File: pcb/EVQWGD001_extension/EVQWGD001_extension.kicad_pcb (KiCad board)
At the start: 2 copper layers, 16.8 x 19.3 mm, 6 parts, among them J1 Conn_01x01_MountingPin, J2 Conn_01x01_MountingPin, J3 Conn_01x01_MountingPin, J4 Conn_01x01_MountingPin, J5 Conn_01x01_MountingPin, SW1 RotaryEncoder_Switch

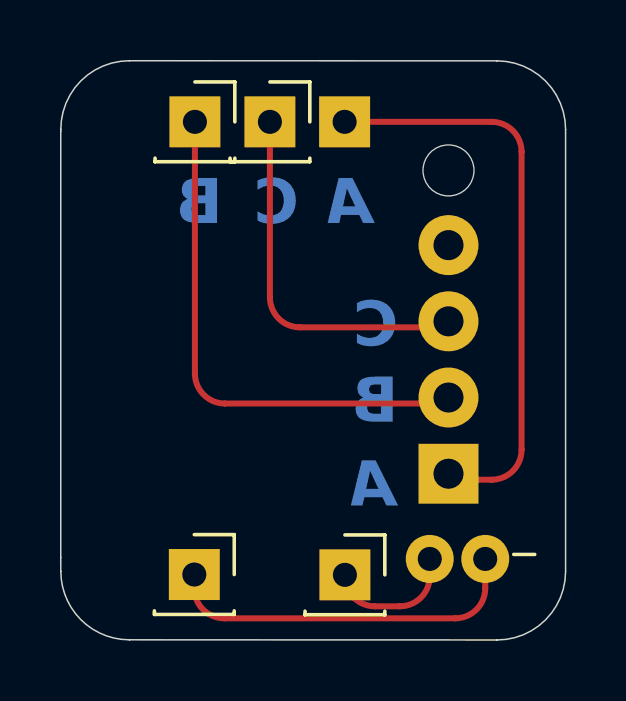
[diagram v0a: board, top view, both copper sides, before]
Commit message: add fp and symbol
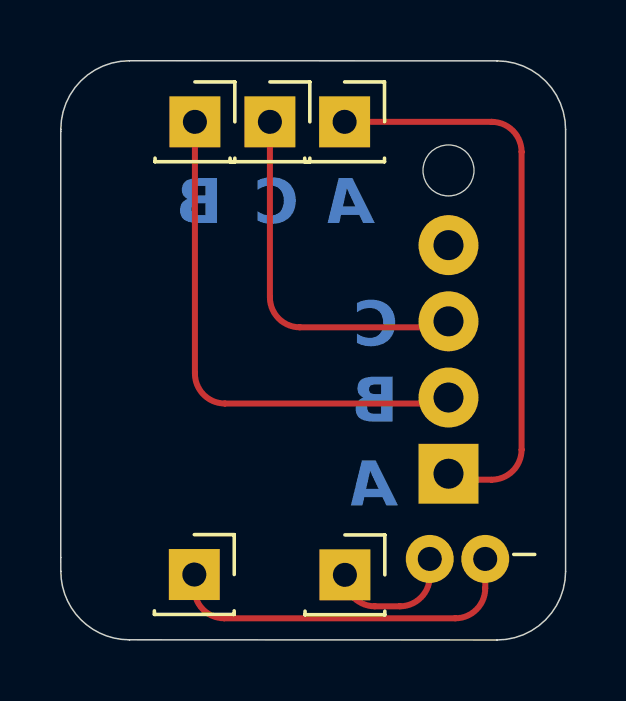
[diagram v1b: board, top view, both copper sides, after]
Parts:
- J1, J2, J3, J4, J5: footprint Connector_PinSocket_2.54mm:PinSocket_1x01_P2.54mm_Vertical -> roBa:PinSocket_1x01_P2.54mm_Vertical
- SW1: footprint EVQWGD001:EVQWGD001 -> roBa:EVQWGD001
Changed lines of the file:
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@@
 	(net 4 "Net-(J4-Pin_1)")
 	(net 5 "Net-(J5-Pin_1)")
-	(footprint "Connector_PinSocket_2.54mm:PinSocket_1x01_P2.54mm_Vertical"
+	(footprint "roBa:PinSocket_1x01_P2.54mm_Vertical"
 		(layer "F.Cu")
 		(at 149.95 93.98)
@@
 			)
 		)
-		(property "Footprint" "Connector_PinSocket_2.54mm:PinSocket_1x01_P2.54mm_Vertical"
+		(property "Footprint" "roBa:PinSocket_1x01_P2.54mm_Vertical"
 			(at 0 0 0)
 			(unlocked yes)
@@
 			)
 		)
+		(property ki_fp_filters "Connector*:*_1x??-1MP*")
+		(sheetname "ルート")
+		(sheetfile "EVQWGD001_extension.kicad_sch")
 		(attr through_hole)
 		(fp_line
@@
 		)
 	)
-	(footprint "Connector_PinSocket_2.54mm:PinSocket_1x01_P2.54mm_Vertical"
+	(footprint "roBa:PinSocket_1x01_P2.54mm_Vertical"
 		(layer "F.Cu")
 		(at 149.93 109.07)
@@
 			)
 		)
-		(property "Footprint" "Connector_PinSocket_2.54mm:PinSocket_1x01_P2.54mm_Vertical"
+		(property "Footprint" "roBa:PinSocket_1x01_P2.54mm_Vertical"
 			(at 0 0 0)
 			(unlocked yes)
@@
 			)
 		)
+		(property ki_fp_filters "Connector*:*_1x??-1MP*")
+		(sheetname "ルート")
+		(sheetfile "EVQWGD001_extension.kicad_sch")
 		(attr through_hole)
 		(fp_line
@@
 		)
 	)
-	(footprint "Connector_PinSocket_2.54mm:PinSocket_1x01_P2.54mm_Vertical"
+	(footprint "roBa:PinSocket_1x01_P2.54mm_Vertical"
 		(layer "F.Cu")
 		(at 152.45 93.98)
@@
 			)
 		)
-		(property "Footprint" "Connector_PinSocket_2.54mm:PinSocket_1x01_P2.54mm_Vertical"
+		(property "Footprint" "roBa:PinSocket_1x01_P2.54mm_Vertical"
 			(at 0 0 0)
 			(unlocked yes)
@@
 			)
 		)
+		(property ki_fp_filters "Connector*:*_1x??-1MP*")
+		(sheetname "ルート")
+		(sheetfile "EVQWGD001_extension.kicad_sch")
 		(attr through_hole)
 		(fp_line
@@
 		)
 	)
-	(footprint "EVQWGD001:EVQWGD001"
+	(footprint "roBa:EVQWGD001"
 		(layer "F.Cu")
 		(at 151.518 101.4 180)
@@
 			)
 		)
-		(property "Footprint" "EVQWGD001:EVQWGD001"
+		(property "Footprint" "roBa:EVQWGD001"
 			(at 1.64 -2.44 0)
 			(unlocked yes)
@@
 			)
 		)
+		(property ki_fp_filters "RotaryEncoder*Switch*")
+		(sheetname "ルート")
+		(sheetfile "EVQWGD001_extension.kicad_sch")
 		(attr through_hole)
 		(fp_line
@@
 		)
 	)
-	(footprint "Connector_PinSocket_2.54mm:PinSocket_1x01_P2.54mm_Vertical"
+	(footprint "roBa:PinSocket_1x01_P2.54mm_Vertical"
 		(layer "F.Cu")
 		(at 154.94 93.98)
@@
 			)
 		)
-		(property "Footprint" "Connector_PinSocket_2.54mm:PinSocket_1x01_P2.54mm_Vertical"
+		(property "Footprint" "roBa:PinSocket_1x01_P2.54mm_Vertical"
 			(at 0 0 0)
 			(unlocked yes)
@@
 			)
 		)
+		(property ki_fp_filters "Connector*:*_1x??-1MP*")
+		(sheetname "ルート")
+		(sheetfile "EVQWGD001_extension.kicad_sch")
 		(attr through_hole)
+		(fp_line
+			(start -1.33 1.21)
+			(end -1.33 1.33)
+			(stroke
+				(width 0.12)
+				(type solid)
+			)
+			(layer "F.SilkS")
+		)
+		(fp_line
+			(start -1.33 1.33)
+			(end 1.33 1.33)
+			(stroke
+				(width 0.12)
+				(type solid)
+			)
+			(layer "F.SilkS")
+		)
+		(fp_line
+			(start 0 -1.33)
+			(end 1.33 -1.33)
+			(stroke
+				(width 0.12)
+				(type solid)
+			)
+			(layer "F.SilkS")
+		)
+		(fp_line
+			(start 1.33 -1.33)
+			(end 1.33 0)
+			(stroke
+				(width 0.12)
+				(type solid)
+			)
+			(layer "F.SilkS")
+		)
+		(fp_line
+			(start 1.33 1.21)
+			(end 1.33 1.33)
+			(stroke
+				(width 0.12)
+				(type solid)
+			)
+			(layer "F.SilkS")
+		)
 		(fp_line
 			(start -1.8 -1.8)
@@
 		)
 	)
-	(footprint "Connector_PinSocket_2.54mm:PinSocket_1x01_P2.54mm_Vertical"
+	(footprint "roBa:PinSocket_1x01_P2.54mm_Vertical"
 		(layer "F.Cu")
 		(at 154.95 109.08)
@@
 			)
 		)
-		(property "Footprint" "Connector_PinSocket_2.54mm:PinSocket_1x01_P2.54mm_Vertical"
+		(property "Footprint" "roBa:PinSocket_1x01_P2.54mm_Vertical"
 			(at 0 0 0)
 			(unlocked yes)
@@
 			)
 		)
+		(property ki_fp_filters "Connector*:*_1x??-1MP*")
+		(sheetname "ルート")
+		(sheetfile "EVQWGD001_extension.kicad_sch")
 		(attr through_hole)
 		(fp_line
